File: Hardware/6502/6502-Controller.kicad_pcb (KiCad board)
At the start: 2 copper layers, 150.5 x 75.1 mm, 36 parts, among them J1 User Port One, J10 5V, J20 Power Switch, J21 Reset, J3 Expanstion Port, J4 Expansion IRQ Enable, J5 6522 IRQ Enable, J6 SERIAL IRQ Enale, J7 SERIAL, J8 Baud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

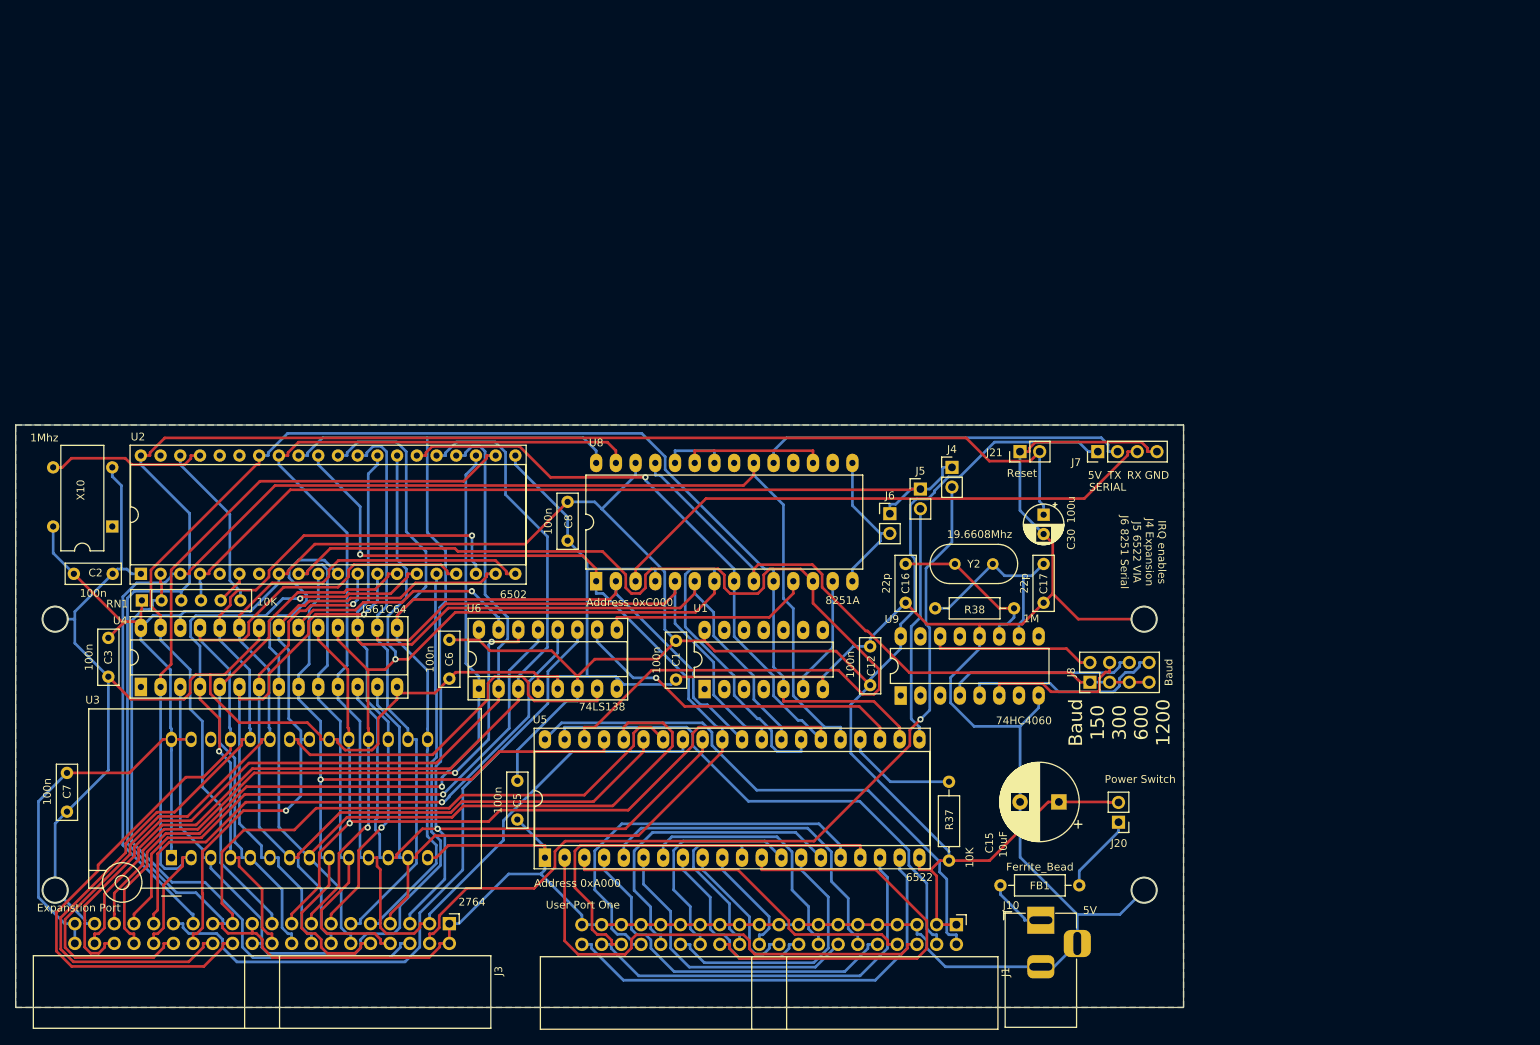
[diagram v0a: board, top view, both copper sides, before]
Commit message: Update of PCB
Updating PCB to newest version, fixing no power light, reset circuit, 8251a reset addition and incorrect 74HC4060 pin out corrections.
Changed address of 8251a from 0xC000 to 0x8000 on PCB.
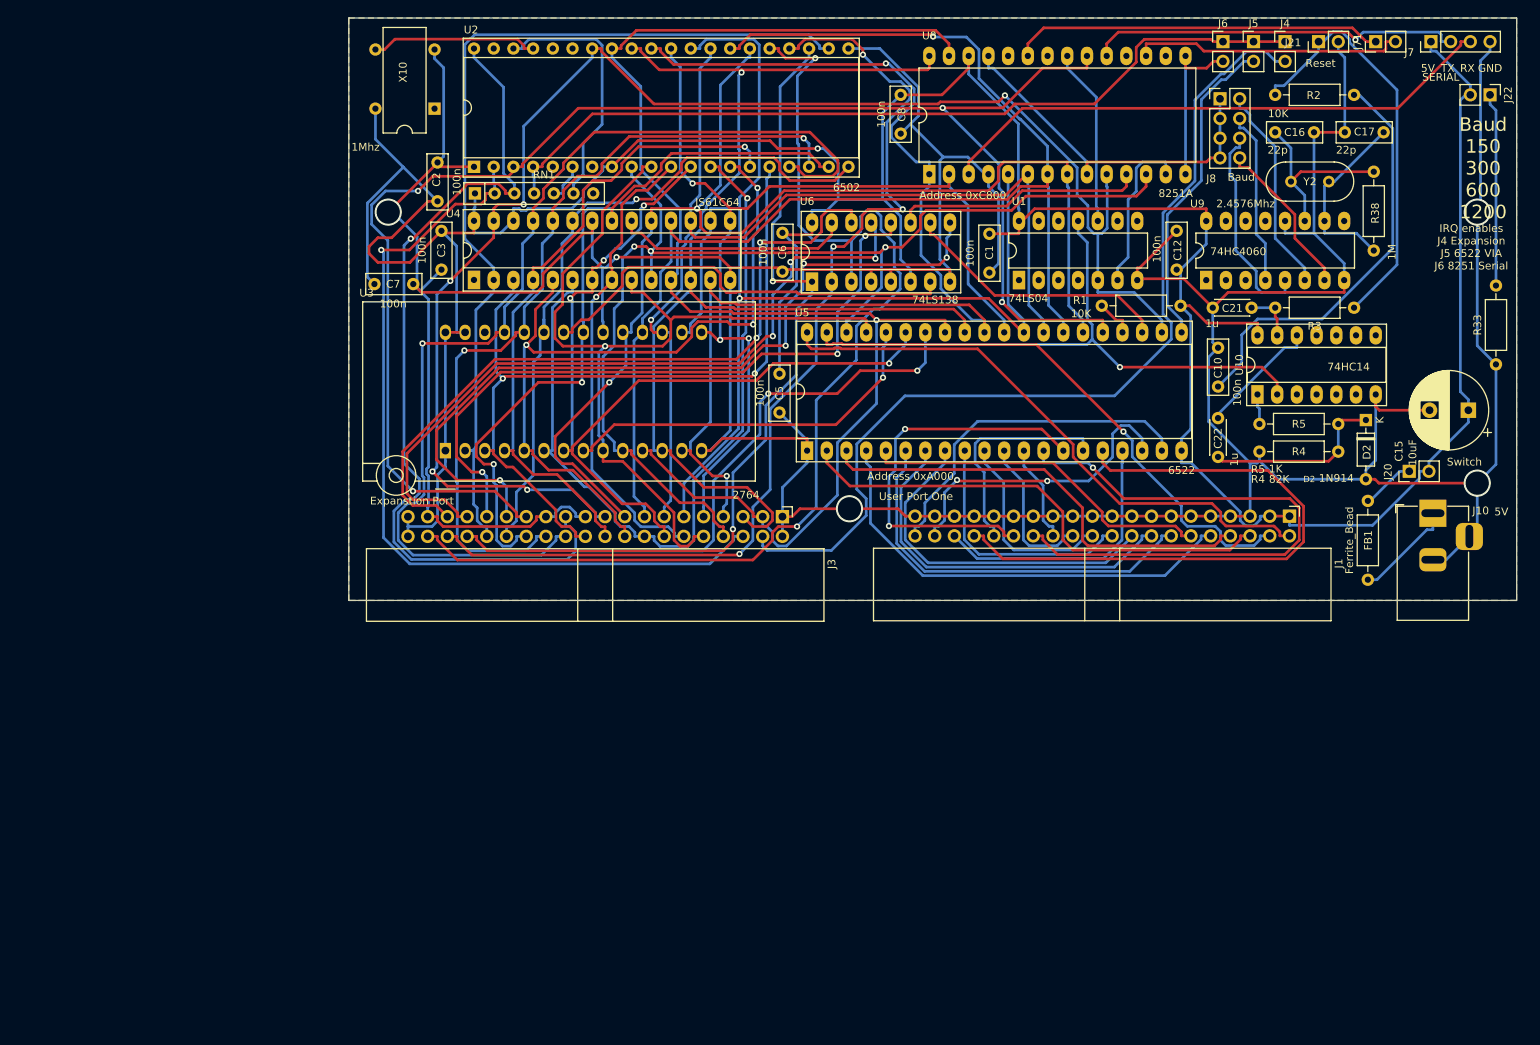
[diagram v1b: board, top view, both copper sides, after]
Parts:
- removed C30: 100u, Capacitor_THT:CP_Radial_D5.0mm_P2.50mm
- added C10: 100n, Capacitor_THT:C_Rect_L7.0mm_W2.5mm_P5.00mm, F.Cu at (195.6, 88.3)
- added C21: 1u, Capacitor_THT:C_Disc_D4.3mm_W1.9mm_P5.00mm, F.Cu at (199.9, 78.1)
- added C22: 1u, Capacitor_THT:C_Disc_D4.3mm_W1.9mm_P5.00mm, F.Cu at (195.6, 92.3)
- added D2: 1N914, Diode_THT:D_DO-35_SOD27_P7.62mm_Horizontal, F.Cu at (214.6, 92.6)
- added J22: LED, Connector_PinHeader_2.54mm:PinHeader_1x02_P2.54mm_Vertical, F.Cu at (230.6, 50.7)
- added J71: RTS/CTS, Connector_PinHeader_2.54mm:PinHeader_1x02_P2.54mm_Vertical, F.Cu at (215.9, 43.8)
- added R2: 10K, Resistor_THT:R_Axial_DIN0207_L6.3mm_D2.5mm_P10.16mm_Horizontal, F.Cu at (213.1, 50.7)
- added R3: 47K, Resistor_THT:R_Axial_DIN0207_L6.3mm_D2.5mm_P10.16mm_Horizontal, F.Cu at (213.1, 78.1)
- added R33: 330R, Resistor_THT:R_Axial_DIN0207_L6.3mm_D2.5mm_P10.16mm_Horizontal, F.Cu at (231.4, 85.4)
- added R4: 82K, Resistor_THT:R_Axial_DIN0207_L6.3mm_D2.5mm_P10.16mm_Horizontal, F.Cu at (211.1, 96.6)
- added R5: 1K, Resistor_THT:R_Axial_DIN0207_L6.3mm_D2.5mm_P10.16mm_Horizontal, F.Cu at (211.1, 93.1)
- added U10: 74HC14, Package_DIP:DIP-14_W7.62mm_Socket_LongPads, F.Cu at (200.7, 89.3)
- J20: value Power Switch -> Switch
- RN1: footprint Resistor_THT:R_Array_SIP6 -> Resistor_THT:R_Array_SIP7
- Y2: value 19.6608Mhz -> 2.4576Mhz
- moved J8 77.0 mm to (195.8, 51.2), turned to 0 degrees
- moved J6 74.5 mm to (196.2, 43.8)
- moved C7 74.4 mm to (86.9, 75.1), turned to 0 degrees
- moved C16 73.2 mm to (202.9, 55.5), turned to 0 degrees
- moved C15 73.0 mm to (227.8, 91.3)
- moved R38 72.9 mm to (215.6, 70.7), turned to 90 degrees
- moved J10 72.8 mm to (223.3, 104.6)
- moved J5 71.9 mm to (200.2, 43.8)
- moved C17 70.8 mm to (216.9, 55.5), turned to 180 degrees
- moved J4 69.7 mm to (204.2, 43.8)
- moved J7 68.1 mm to (223.0, 43.8)
- moved X10 68.0 mm to (94.6, 52.5)
- moved J1 67.9 mm to (204.8, 105.0)
- moved C3 67.8 mm to (95.5, 68.2)
- moved U6 67.8 mm to (143.3, 74.8)
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- renumbered R37 to R1
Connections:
- J21 pad 1: GND -> Net-(J21-Pad1)
- J21 pad 2: ~RES -> GND
- J3 pad 29: 0x8000 -> 0xC000
- U1 pad 10: (no net) -> Net-(U1-Pad10)
- U1 pad 11: (no net) -> ~RES
- U6 pad 11: 0x8000 -> ~8251_EN
- U6 pad 9: ~8251_EN -> 0xC000
- U8 pad 17: Net-(U8-Pad17) -> Net-(J71-Pad2)
- U8 pad 21: (no net) -> Net-(U1-Pad10)
- U8 pad 22: Net-(U8-Pad22) -> (no net)
- U8 pad 23: Net-(U8-Pad17) -> Net-(J71-Pad1)
- U8 pad 24: Net-(U8-Pad22) -> (no net)
- U9 pad 14: B150 -> (no net)
- U9 pad 4: B600 -> B300
- U9 pad 5: B1200 -> B600
- U9 pad 6: B300 -> B150
- U9 pad 7: (no net) -> B1200
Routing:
- net 0xC000: track 0.00 -> 102.8 mm, vias 0 -> 4
- net 0x8000: track 84.8 -> 0.00 mm
- net Net-(J21-Pad1): track 0.00 -> 54.4 mm
- net /A0: track 205.4 -> 151.1 mm, vias 0 -> 3
- net Net-(C10-Pad1): track 0.00 -> 54.2 mm
- net 5V: track 402.0 -> 456.0 mm, vias 0 -> 1
- net GND: track 559.6 -> 613.0 mm, vias 4 -> 5
- net /PB3: track 29.1 -> 77.4 mm, vias 0 -> 1
- net Net-(J71-Pad1): track 0.00 -> 48.0 mm
- net /PB2: track 57.4 -> 12.8 mm
- net ~RES: track 280.8 -> 241.6 mm, vias 0 -> 4
- net Net-(J71-Pad2): track 0.00 -> 35.2 mm
- net /A4: track 69.0 -> 103.6 mm
- net Net-(J8-Pad1): track 80.8 -> 47.4 mm
- net /A15: track 117.9 -> 147.5 mm, vias 0 -> 2
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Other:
- board text added: "A0, D2"
- board text added: "A1, D3"
- board text added: "A2, D4"
- board text added: "A3, D5"
- board text added: "A4, D6"
- board text added: "A5, D7"
- board text added: "A6, R~W"
- board text added: "Address 0xC800"
- board text added: "CA1"
- board text added: "CA2"
- board text added: "CB1"
- board text added: "CB2"
- board text added: "GND x 2"
- board text added: "IRQ, D0"
- board text added: "PA0"
- board text added: "PA1"
- board text added: "PA2"
- board text added: "PA3"
- board text added: "PA4"
- board text added: "PA5"
- board text added: "PA6"
- board text added: "PA7"
- board text added: "PB0"
- board text added: "PB1"
- board text added: "PB2"
- board text added: "PB3"
- board text added: "PB4"
- board text added: "PB5"
- board text added: "PB6"
- board text added: "PB7"
- board text added: "RDY, D1"
- board text removed: "Address 0xC000"

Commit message: 6502 project update
Added Gerber's, PCB and updated schematic with single step (not on PCB)
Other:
- board text added: "12"
- board text added: "15"
- board text added: "2"
- board text added: "2764 or AT28C64"
- board text added: "30"
- board text added: "4"
- board text added: "6"
- board text added: "60"
- board text added: "A11, C"
- board text added: "A13"
- board text added: "A14"
- board text added: "A15"
- board text added: "Address 0x8000"
- board text added: "Addresses, ACI on 0xC000 0x2000, 0x4000, 0x6000, 0xC000"
- board text added: "C"
- board text added: "P"
- board text added: "RAM"
- board text added: "ROM"
- board text added: "S"
- board text removed: "A11, 8"
- board text removed: "Address 0xC800"
- board text removed: "Baud 150 300 600 1200"

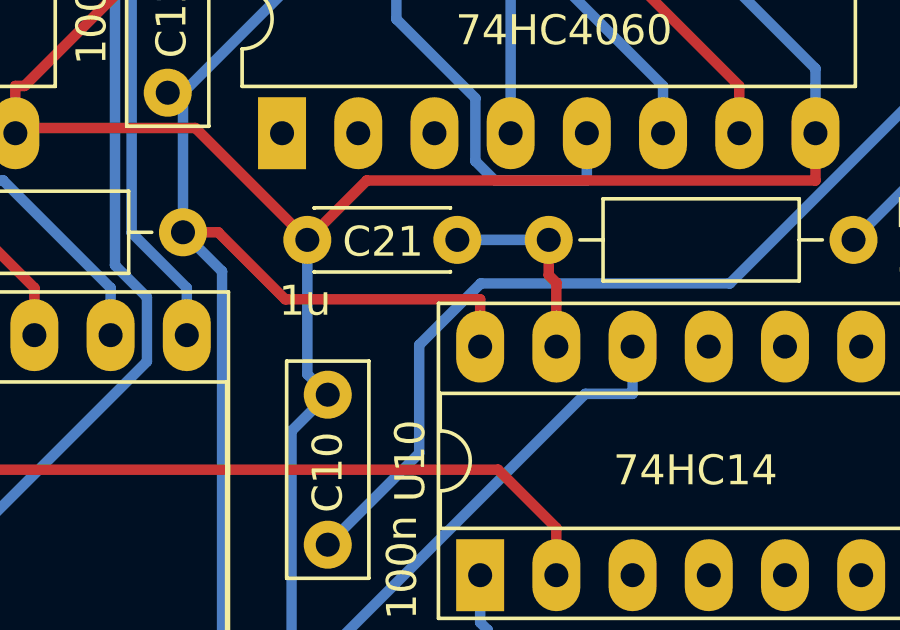
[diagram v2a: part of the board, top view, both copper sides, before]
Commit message: Fixed R2 issue
Fixed issue with R2 not having a connection to 5V rail
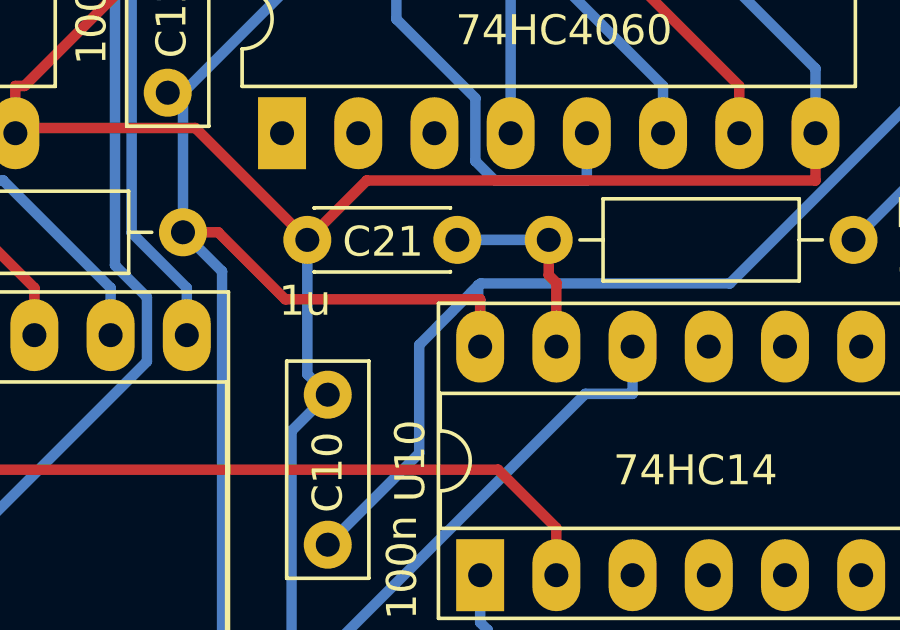
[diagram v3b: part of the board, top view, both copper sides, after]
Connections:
- C10 pad 1: Net-(C10-Pad1) -> 5V
- R2 pad 1: Net-(C10-Pad1) -> 5V
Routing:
- net 5V: track 456.0 -> 512.3 mm
- net Net-(C10-Pad1): track 54.2 -> 0.00 mm

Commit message: Version 2 silkscreen
Update of silkscreen to indicate version2
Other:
- board text added: "6502 - VIA, V1.1 board Version 2"
- board text removed: "6502 - VIA, V1.1 board Version 1"
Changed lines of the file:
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@@
   (page A4)
   (layers
-    (0 F.Cu signal)
-    (31 B.Cu signal)
+    (0 F.Cu signal hide)
+    (31 B.Cu signal hide)
     (32 B.Adhes user)
     (33 F.Adhes user)
@@
     (add_net "Net-(RN1-Pad6)")
     (add_net "Net-(U1-Pad10)")
-    (add_net "Net-(U2-Pad39)")
-    (add_net "Net-(U3-Pad26)")
-    (add_net "Net-(U8-Pad16)")
-    (add_net "Net-(U8-Pad22)")
-    (add_net "Net-(U8-Pad24)")
-    (add_net "Net-(U9-Pad1)")
-    (add_net "Net-(U9-Pad13)")
-    (add_net "Net-(U9-Pad14)")
-    (add_net "Net-(U9-Pad15)")
-    (add_net "Net-(U9-Pad2)")
-    (add_net "Net-(U9-Pad3)")
-    (add_net "Net-(U9-Pad9)")
-    (add_net "Net-(X10-Pad1)")
     (add_net RDY)
     (add_net R~W)
-    (add_net SYNC)
     (add_net ~6522_EN)
     (add_net ~8251_EN)
@@
     (effects (font (size 1 1) (thickness 0.15)))
   )
-  (gr_text "6502 - VIA, V1.1 \nboard Version 1" (at 174.752 52.959) (layer B.SilkS)
+  (gr_text "6502 - VIA, V1.1 \nboard Version 2" (at 174.752 52.959) (layer B.SilkS)
     (effects (font (size 2 2) (thickness 0.4)) (justify mirror))
   )
@@
   (segment (start 91.44 72.263) (end 95.504 68.199) (width 0.35) (layer F.Cu) (net 2))
   (segment (start 87.3125 72.263) (end 91.44 72.263) (width 0.35) (layer F.Cu) (net 2))
+  (segment (start 213.106 50.673) (end 213.7781 50.673) (width 0.35) (layer B.Cu) (net 2))
+  (segment (start 213.7781 50.673) (end 218.0966 54.9915) (width 0.35) (layer B.Cu) (net 2))
+  (segment (start 218.0966 54.9915) (end 218.0966 70.4439) (width 0.35) (layer B.Cu) (net 2))
+  (segment (start 218.0966 70.4439) (end 208.9845 79.556) (width 0.35) (layer B.Cu) (net 2))
+  (segment (start 208.9845 79.556) (end 200.6805 79.556) (width 0.35) (layer B.Cu) (net 2))
+  (segment (start 198.6285 81.608) (end 198.6285 85.2165) (width 0.35) (layer B.Cu) (net 2))
+  (segment (start 198.6285 85.2165) (end 195.58 88.265) (width 0.35) (layer B.Cu) (net 2))
+  (segment (start 200.66 80.111) (end 200.5965 80.0475) (width 0.35) (layer B.Cu) (net 2))
+  (segment (start 200.5965 80.0475) (end 200.5965 79.6163) (width 0.35) (layer B.Cu) (net 2))
+  (segment (start 200.66 81.661) (end 200.66 80.111) (width 0.35) (layer B.Cu) (net 2))
+  (segment (start 200.6805 79.556) (end 200.5965 79.6163) (width 0.35) (layer B.Cu) (net 2))
+  (segment (start 200.5965 79.6163) (end 198.6285 81.608) (width 0.35) (layer B.Cu) (net 2))
   (segment (start 204.978 61.849) (end 206.248 60.579) (width 0.35) (layer F.Cu) (net 3))
   (segment (start 206.248 60.579) (end 215.646 60.579) (width 0.35) (layer F.Cu) (net 3))
@@
   (segment (start 218.9927 99.187) (end 215.1827 102.997) (width 0.35) (layer B.Cu) (net 76))
   (segment (start 215.1827 102.997) (end 214.884 102.997) (width 0.35) (layer B.Cu) (net 76))
-  (segment (start 213.106 50.673) (end 213.7781 50.673) (width 0.35) (layer B.Cu) (net 2))
-  (segment (start 213.7781 50.673) (end 218.0966 54.9915) (width 0.35) (layer B.Cu) (net 2))
-  (segment (start 218.0966 54.9915) (end 218.0966 70.4439) (width 0.35) (layer B.Cu) (net 2))
-  (segment (start 218.0966 70.4439) (end 208.9845 79.556) (width 0.35) (layer B.Cu) (net 2))
-  (segment (start 208.9845 79.556) (end 200.6805 79.556) (width 0.35) (layer B.Cu) (net 2))
-  (segment (start 198.6285 81.608) (end 198.6285 85.2165) (width 0.35) (layer B.Cu) (net 2))
-  (segment (start 198.6285 85.2165) (end 195.58 88.265) (width 0.35) (layer B.Cu) (net 2))
-  (segment (start 200.66 80.111) (end 200.5965 80.0475) (width 0.35) (layer B.Cu) (net 2))
-  (segment (start 200.5965 80.0475) (end 200.5965 79.6163) (width 0.35) (layer B.Cu) (net 2))
-  (segment (start 200.66 81.661) (end 200.66 80.111) (width 0.35) (layer B.Cu) (net 2))
-  (segment (start 200.6805 79.556) (end 200.5965 79.6163) (width 0.35) (layer B.Cu) (net 2))
-  (segment (start 200.5965 79.6163) (end 198.6285 81.608) (width 0.35) (layer B.Cu) (net 2))
   (segment (start 199.898 78.105) (end 202.946 78.105) (width 0.35) (layer B.Cu) (net 77))
   (segment (start 202.946 78.105) (end 202.946 79.2803) (width 0.35) (layer F.Cu) (net 77))
